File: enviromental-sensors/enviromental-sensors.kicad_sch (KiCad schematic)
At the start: 45 parts, among them IC1 ESP32-C3-WROOM-02-N4, IC2 TPS2117DRLR, J1 USB_C_Receptacle_USB2.0, J2 S2B-PH-SM4-TB_LF__SN_, J3 FH52-10S-0.5SH_99, J4 Conn_01x02_Socket, Q1 AO3401A, SW1 TC-0522C-1.7-160G, SW2 TC-0522C-1.7-160G, SW3 TC-0522C-1.7-160G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

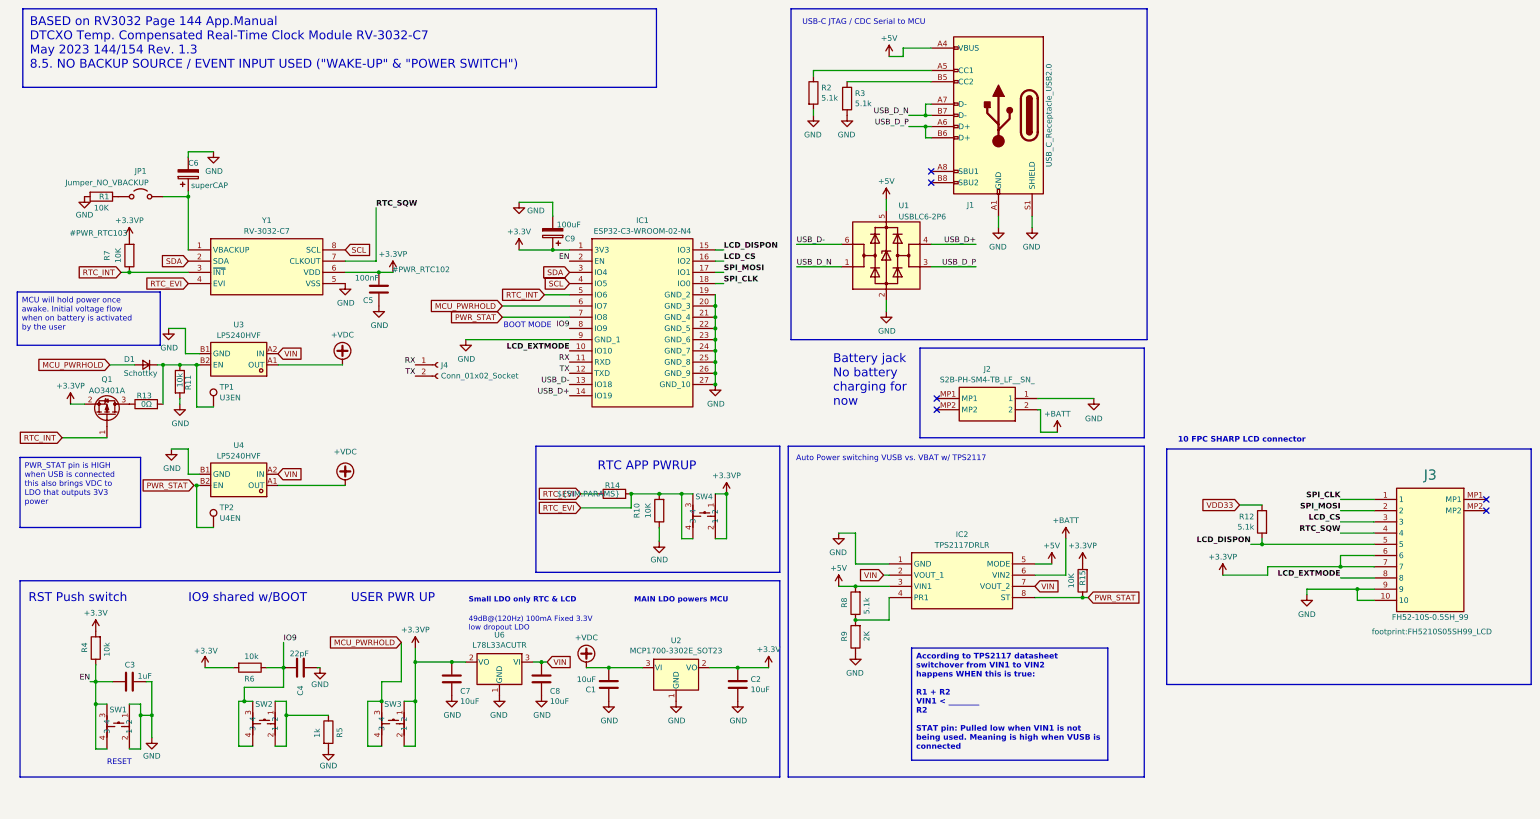
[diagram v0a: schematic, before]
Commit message: Add env. sensors PCB
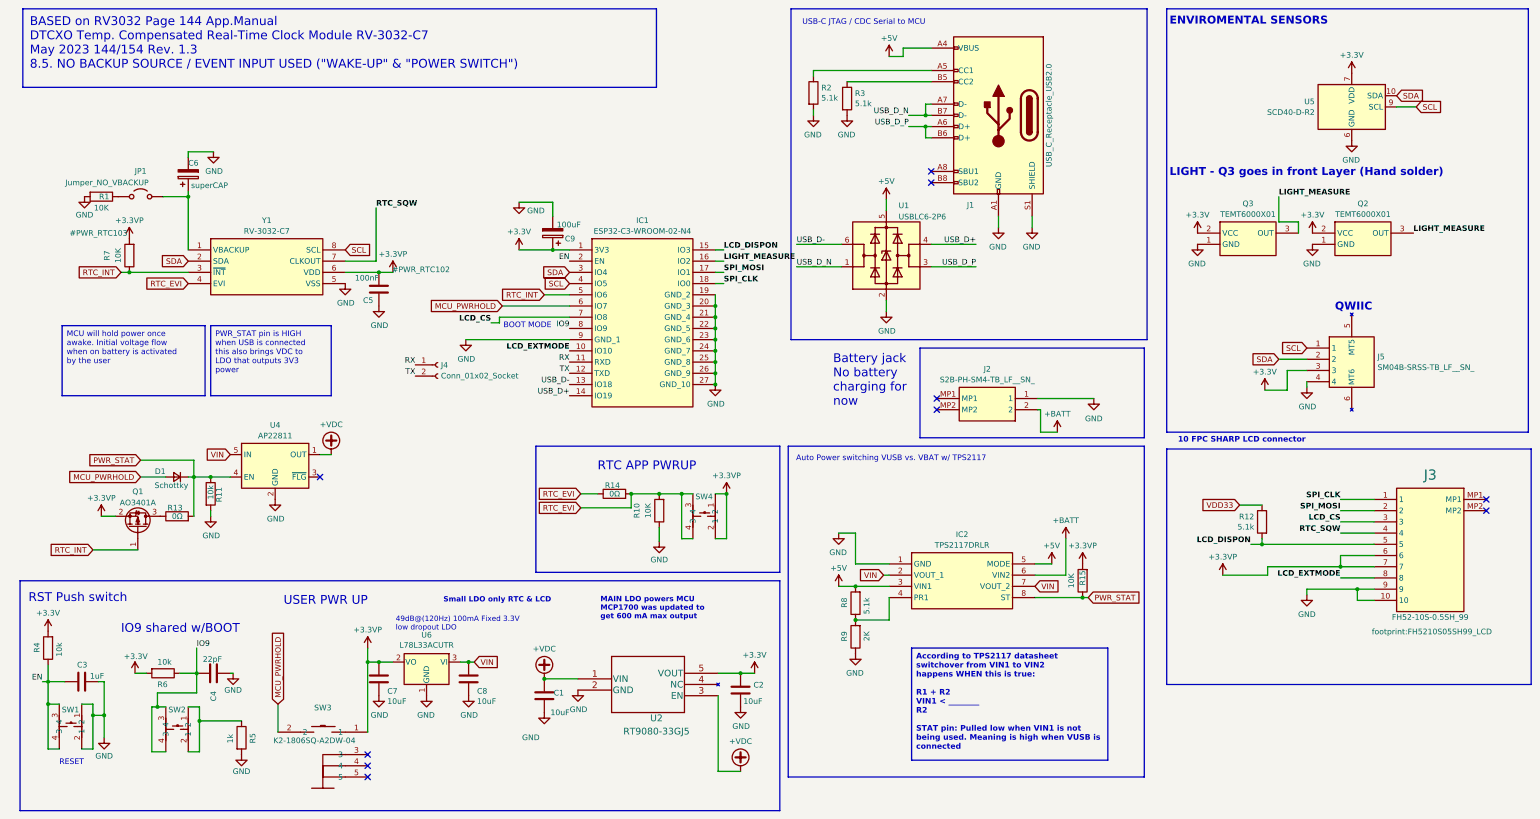
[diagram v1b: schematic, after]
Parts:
- removed SW3: TC-0522C-1.7-160G, footprint:C2845289_SW-SMD_4P-L5.2-W5.2-P3.70-LS6.4, symbol BUTTON:TC-0522C-1.7-160G
- removed TP1: U3EN, TestPoint:TestPoint_Pad_D1.5mm, symbol Connector:TestPoint
- removed TP2: U4EN, TestPoint:TestPoint_Pad_D1.5mm, symbol Connector:TestPoint
- removed U2: MCP1700-3302E_SOT23, Package_TO_SOT_SMD:SOT-23, symbol epaper-breakout-rescue:MCP1700-3302E_SOT23-Regulator_Linear
- removed U3, U4: LP5240HVF, footprint:C2890373_WLCSP-4, symbol easyeda:LP5240HVF
- added J5: SM04B-SRSS-TB_LF__SN_, enviromental:QWIIC_SM04B-SRSS-TB_LFSN_, symbol QWIIC:SM04B-SRSS-TB_LF__SN_
- added Q2, Q3: TEMT6000X01, enviromental:TEMT6000X01, symbol SENSOR_LIGHT:TEMT6000X01
- added SW3: K2-1806SQ-A2DW-04, enviromental:C5143621_KEY-SMD_TS24ZJ, symbol side-button:K2-1806SQ-A2DW-04
- added U2: RT9080-33GJ5, Package_TO_SOT_SMD:TSOT-23-5, symbol epdiy:RT9080-33GJ5
- added U4: AP22811, enviromental:C3001660_SOT95P285X140-5N, symbol Power_Management:AP22804AW5
- added U5: SCD40-D-R2, Sensor:Sensirion_SCD4x-1EP_10.1x10.1mm_P1.25mm_EP4.8x4.8mm, symbol Sensor_Gas:SCD40-D-R2
- R14: value ${SIM.PARAMS} -> 0Ω
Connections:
- net +3.3V: now also J5.3, Q2.2 (VCC), Q3.2 (VCC), U2.5 (VOUT), U5.19 (VDD), U5.7 (VDD)
- net +3.3VP: now also SW3.1
- net +VDC: now also U2.1 (VIN), U2.3 (EN), U4.1 (OUT)
- net GND: now also J5.4, Q2.1 (GND), Q3.1 (GND), U2.2 (GND), U4.2 (GND), U5.20 (GND), U5.21 (GND), U5.6 (GND)
- net LCD_CS: now also IC1.7 (IO8); no longer IC1.16 (IO2)
- net MCU_PWRHOLD: now also SW3.2
- net PWR_STAT: now also D1.1 (K), R11.1, R13.2, U4.4 (EN); no longer IC1.7 (IO8)
- net SCL: now also J5.1, U5.9 (SCL)
- net SDA: now also J5.2, U5.10 (SDA)
- net VIN: now also U4.5 (IN)
- new net LIGHT_MEASURE: IC1.16 (IO2), Q2.3 (OUT), Q3.3 (OUT)
- no-connect marks 6 -> 10
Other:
- note added: "ENVIROMENTAL SENSORS"
- note added: "LIGHT - Q3 goes in front Layer (Hand solder)"
- note added: "MAIN LDO powers MCU MCP1700 was updated to get 600 mA max output"
- note added: "QWIIC"
- note removed: "MAIN LDO powers MCU"
- moved on the sheet: C1, C2, C3, C4, C7, C8, D1, Q1, R11, R13, R4, R5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

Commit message: 1.0 fixes: QWIIC corrected (note 1.0 release before this commit is unfixed)
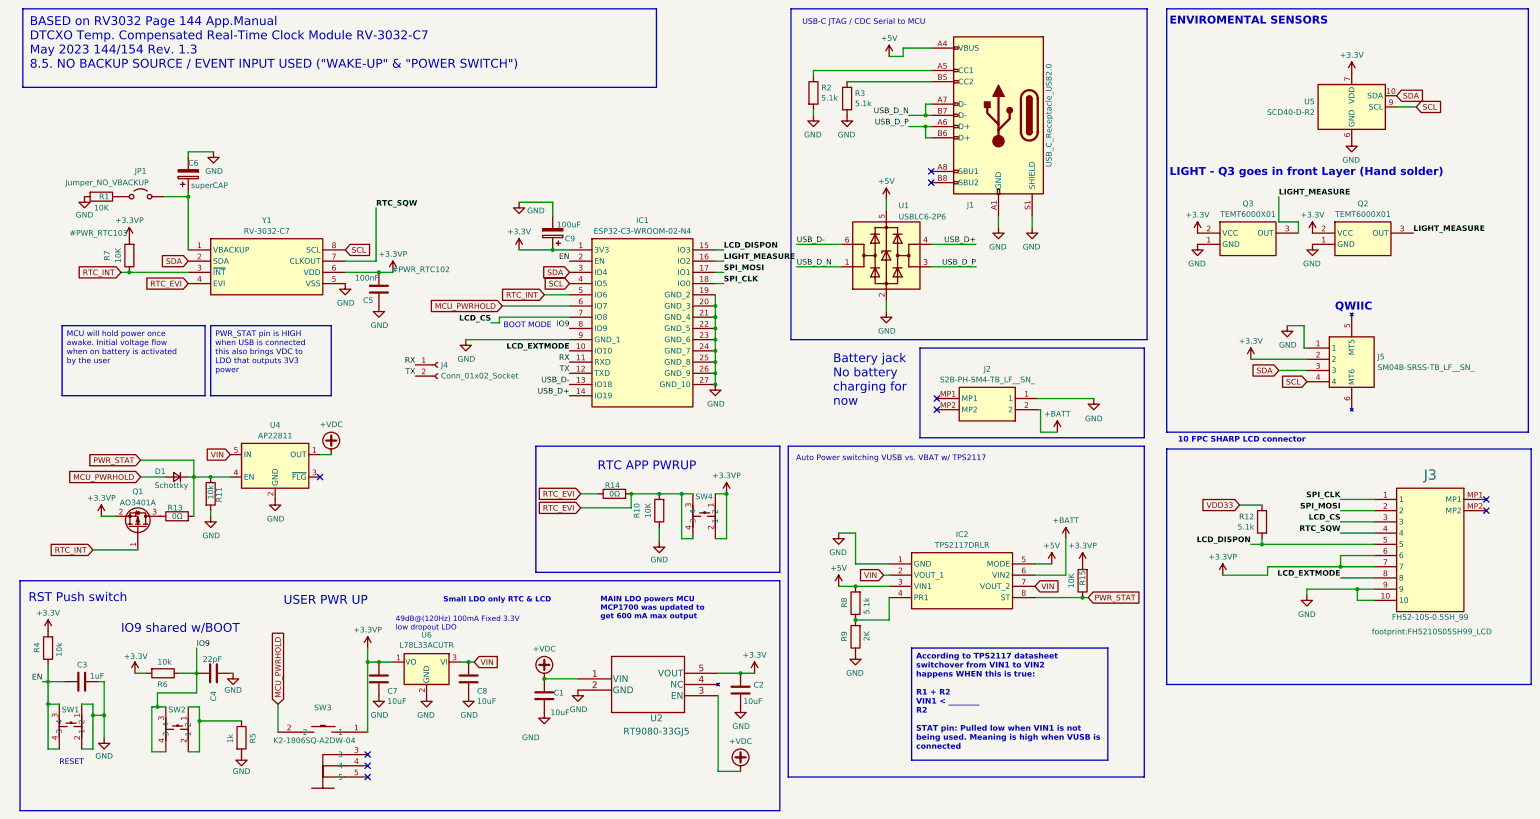
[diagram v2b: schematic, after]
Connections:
- net +3.3V: now also J5.2; no longer J5.3
- net +3.3VP: now also U6.1 (VO); no longer U6.2 (VO)
- net GND: now also J5.1, U6.2 (GND); no longer J5.4, U6.1 (GND)
- net SCL: now also J5.4; no longer J5.1
- net SDA: now also J5.3; no longer J5.2
